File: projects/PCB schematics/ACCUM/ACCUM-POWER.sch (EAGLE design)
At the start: 9 parts, among them J1 2P(90DEG)_1-770966-0, J2 2P(90DEG)_1-770966-0, J3 2P(90DEG)_1-770966-0

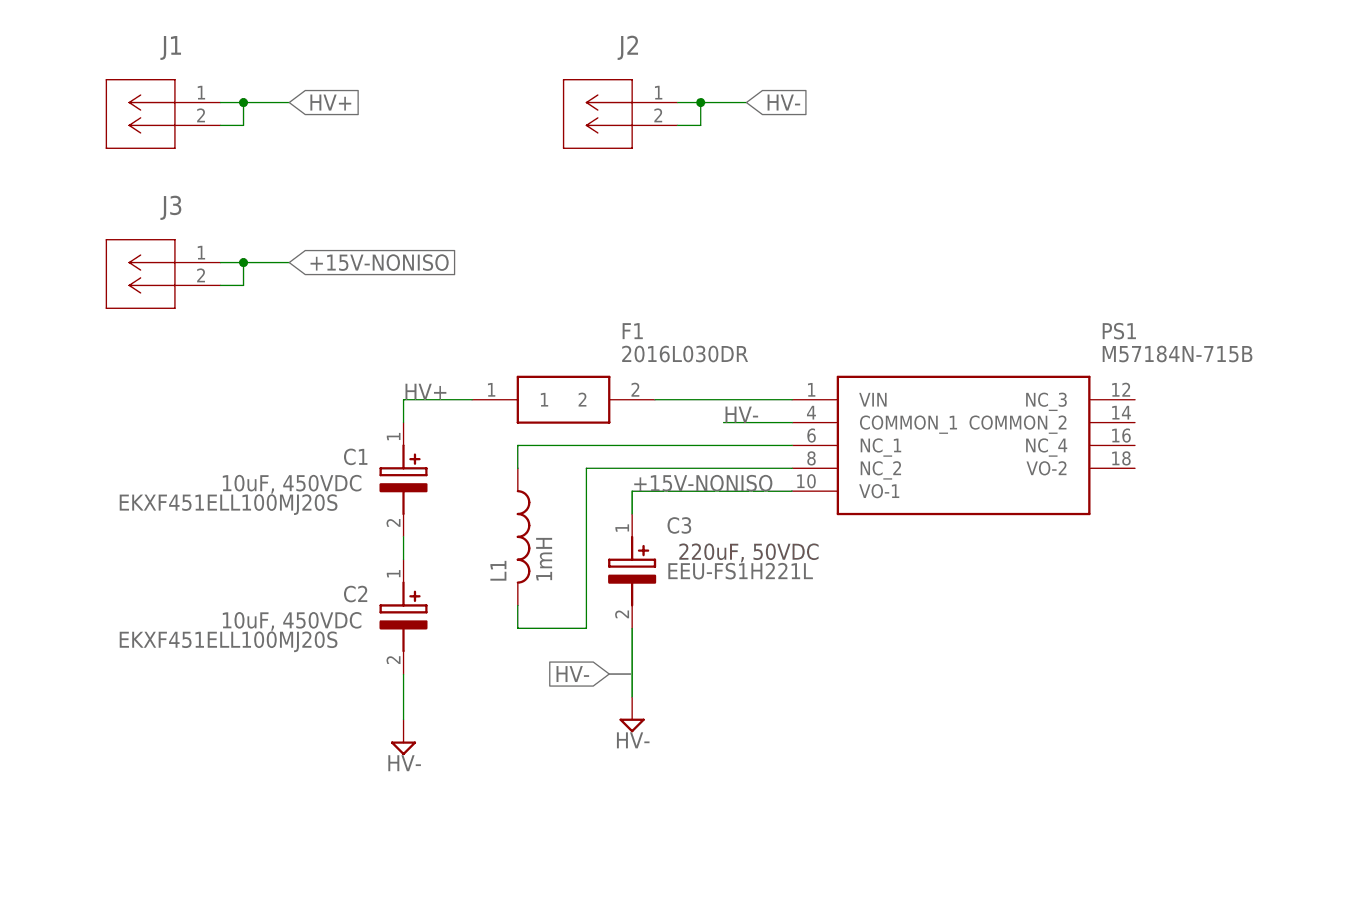
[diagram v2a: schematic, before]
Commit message: TSAL - Added in fuses.
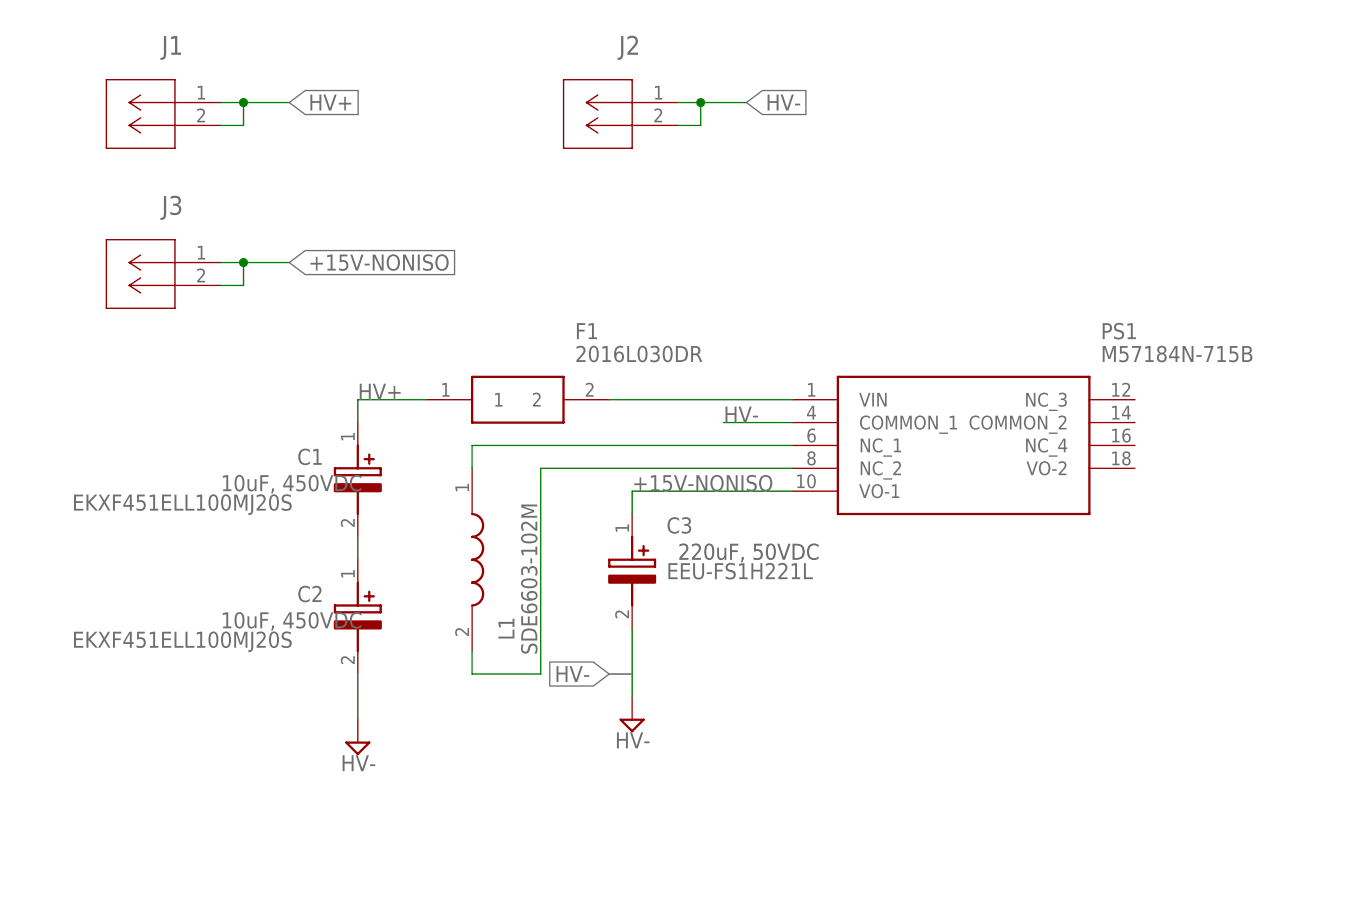
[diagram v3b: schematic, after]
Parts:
- L1: value 1mH -> SDE6603-102M; device rcl:L-USL2012C -> SDE6603-102M:SDE6603-102M
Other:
- moved on the sheet: C1, C2, F1
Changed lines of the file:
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@@
 <parts>
 <part name="PS1" library="M57184N-715B" deviceset="M57184N-715B" device=""/>
-<part name="L1" library="rcl" library_urn="urn:adsk.eagle:library:334" deviceset="L-US" device="L2012C" package3d_urn="urn:adsk.eagle:package:23475/2" value="1mH"/>
 <part name="C3" library="EEU-FS1H221L" deviceset="EEU-FS1H221L" device=""/>
 <part name="SUPPLY16" library="supply2" library_urn="urn:adsk.eagle:library:372" deviceset="GND" device="" value="HV-"/>
@@
 <part name="J3" library="con-MATE-N-LOK" deviceset="2P(90DEG)_1-770966-0" device=""/>
 <part name="F1" library="SamacSys_Parts" deviceset="2016L030DR" device=""/>
+<part name="L1" library="SDE6603-102M" deviceset="SDE6603-102M" device=""/>
 </parts>
 <sheets>
@@
 <attribute name="VALUE" x="118.11" y="63.5" size="1.778" layer="96" align="center-left"/>
 </instance>
-<instance part="L1" gate="G$1" x="53.34" y="43.18" smashed="yes">
-<attribute name="NAME" x="52.07" y="38.1" size="1.778" layer="95" rot="R90"/>
-<attribute name="VALUE" x="57.15" y="38.1" size="1.778" layer="96" rot="R90"/>
-</instance>
 <instance part="C3" gate="G$1" x="66.04" y="45.72" smashed="yes" rot="R270">
 <attribute name="NAME" x="69.85" y="44.45" size="1.778" layer="95" rot="MR180" align="center-left"/>
@@
 <attribute name="VALUE" x="64.135" y="19.685" size="1.778" layer="96"/>
 </instance>
-<instance part="SUPPLY17" gate="GND" x="40.64" y="20.32" smashed="yes">
-<attribute name="VALUE" x="38.735" y="17.145" size="1.778" layer="96"/>
+<instance part="SUPPLY17" gate="GND" x="35.56" y="20.32" smashed="yes">
+<attribute name="VALUE" x="33.655" y="17.145" size="1.778" layer="96"/>
 </instance>
-<instance part="C1" gate="G$1" x="40.64" y="55.88" smashed="yes" rot="R270">
-<attribute name="NAME" x="36.83" y="52.07" size="1.778" layer="95" rot="R180" align="center-left"/>
-<attribute name="VALUE" x="8.89" y="46.99" size="1.778" layer="96" align="center-left"/>
+<instance part="C1" gate="G$1" x="35.56" y="55.88" smashed="yes" rot="R270">
+<attribute name="NAME" x="31.75" y="52.07" size="1.778" layer="95" rot="R180" align="center-left"/>
+<attribute name="VALUE" x="3.81" y="46.99" size="1.778" layer="96" align="center-left"/>
 </instance>
-<instance part="C2" gate="G$1" x="40.64" y="40.64" smashed="yes" rot="R270">
-<attribute name="NAME" x="36.83" y="36.83" size="1.778" layer="95" rot="R180" align="center-left"/>
-<attribute name="VALUE" x="8.89" y="31.75" size="1.778" layer="96" align="center-left"/>
+<instance part="C2" gate="G$1" x="35.56" y="40.64" smashed="yes" rot="R270">
+<attribute name="NAME" x="31.75" y="36.83" size="1.778" layer="95" rot="R180" align="center-left"/>
+<attribute name="VALUE" x="3.81" y="31.75" size="1.778" layer="96" align="center-left"/>
 </instance>
 <instance part="J1" gate="A" x="20.32" y="91.44" smashed="yes" rot="MR0">
@@
 <attribute name="NAME" x="16.1544" y="78.9686" size="2.0828" layer="95" ratio="6" rot="SMR0"/>
 </instance>
-<instance part="F1" gate="G$1" x="48.26" y="58.42" smashed="yes">
-<attribute name="NAME" x="64.77" y="66.04" size="1.778" layer="95" align="center-left"/>
-<attribute name="VALUE" x="64.77" y="63.5" size="1.778" layer="96" align="center-left"/>
+<instance part="F1" gate="G$1" x="43.18" y="58.42" smashed="yes">
+<attribute name="NAME" x="59.69" y="66.04" size="1.778" layer="95" align="center-left"/>
+<attribute name="VALUE" x="59.69" y="63.5" size="1.778" layer="96" align="center-left"/>
+</instance>
+<instance part="L1" gate="G$1" x="48.26" y="50.8" smashed="yes" rot="R270">
+<attribute name="NAME" x="52.07" y="34.29" size="1.778" layer="95" rot="R270" align="center-left"/>
+<attribute name="VALUE" x="54.61" y="46.99" size="1.778" layer="96" rot="R270" align="center-left"/>
 </instance>
 </instances>
@@
 <segment>
 <pinref part="SUPPLY17" gate="GND" pin="GND"/>
-<wire x1="40.64" y1="22.86" x2="40.64" y2="27.94" width="0.1524" layer="91"/>
+<wire x1="35.56" y1="22.86" x2="35.56" y2="27.94" width="0.1524" layer="91"/>
 <pinref part="C2" gate="G$1" pin="-"/>
 </segment>
@@
 <net name="HV+" class="0">
 <segment>
-<label x="40.64" y="58.42" size="1.778" layer="95"/>
-<wire x1="40.64" y1="58.42" x2="40.64" y2="55.88" width="0.1524" layer="91"/>
+<label x="35.56" y="58.42" size="1.778" layer="95"/>
+<wire x1="35.56" y1="58.42" x2="35.56" y2="55.88" width="0.1524" layer="91"/>
 <pinref part="C1" gate="G$1" pin="+"/>
 <pinref part="F1" gate="G$1" pin="1"/>
-<wire x1="48.26" y1="58.42" x2="40.64" y2="58.42" width="0.1524" layer="91"/>
+<wire x1="43.18" y1="58.42" x2="35.56" y2="58.42" width="0.1524" layer="91"/>
 </segment>
 <segment>
@@
 <net name="N$1" class="0">
 <segment>
+<wire x1="48.26" y1="30.48" x2="48.26" y2="27.94" width="0.1524" layer="91"/>
+<wire x1="48.26" y1="27.94" x2="55.88" y2="27.94" width="0.1524" layer="91"/>
+<wire x1="55.88" y1="27.94" x2="55.88" y2="50.8" width="0.1524" layer="91"/>
+<pinref part="PS1" gate="G$1" pin="NC_2"/>
+<wire x1="55.88" y1="50.8" x2="83.82" y2="50.8" width="0.1524" layer="91"/>
 <pinref part="L1" gate="G$1" pin="2"/>
-<wire x1="53.34" y1="35.56" x2="53.34" y2="33.02" width="0.1524" layer="91"/>
-<wire x1="53.34" y1="33.02" x2="60.96" y2="33.02" width="0.1524" layer="91"/>
-<wire x1="60.96" y1="33.02" x2="60.96" y2="50.8" width="0.1524" layer="91"/>
-<pinref part="PS1" gate="G$1" pin="NC_2"/>
-<wire x1="60.96" y1="50.8" x2="83.82" y2="50.8" width="0.1524" layer="91"/>
 </segment>
 </net>
@@
 <segment>
 <pinref part="PS1" gate="G$1" pin="NC_1"/>
-<wire x1="83.82" y1="53.34" x2="53.34" y2="53.34" width="0.1524" layer="91"/>
+<wire x1="83.82" y1="53.34" x2="48.26" y2="53.34" width="0.1524" layer="91"/>
+<wire x1="48.26" y1="53.34" x2="48.26" y2="50.8" width="0.1524" layer="91"/>
 <pinref part="L1" gate="G$1" pin="1"/>
-<wire x1="53.34" y1="53.34" x2="53.34" y2="50.8" width="0.1524" layer="91"/>
 </segment>
 </net>
@@
 <net name="N$3" class="0">
 <segment>
-<wire x1="40.64" y1="43.18" x2="40.64" y2="40.64" width="0.1524" layer="91"/>
+<wire x1="35.56" y1="43.18" x2="35.56" y2="40.64" width="0.1524" layer="91"/>
 <pinref part="C1" gate="G$1" pin="-"/>
 <pinref part="C2" gate="G$1" pin="+"/>
@@
 <pinref part="F1" gate="G$1" pin="2"/>
 <pinref part="PS1" gate="G$1" pin="VIN"/>
-<wire x1="68.58" y1="58.42" x2="83.82" y2="58.42" width="0.1524" layer="91"/>
+<wire x1="63.5" y1="58.42" x2="83.82" y2="58.42" width="0.1524" layer="91"/>
 </segment>
 </net>
@@
 will not be understood (or retained) with this version.
 </note>
-<note version="8.3" severity="warning">
-Since Version 8.3, EAGLE supports the association of 3D packages
-with devices in libraries, schematics, and board files. Those 3D
-packages will not be understood (or retained) with this version.
-</note>
 </compatibility>

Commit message: ACCUM - Added IMD fuses.
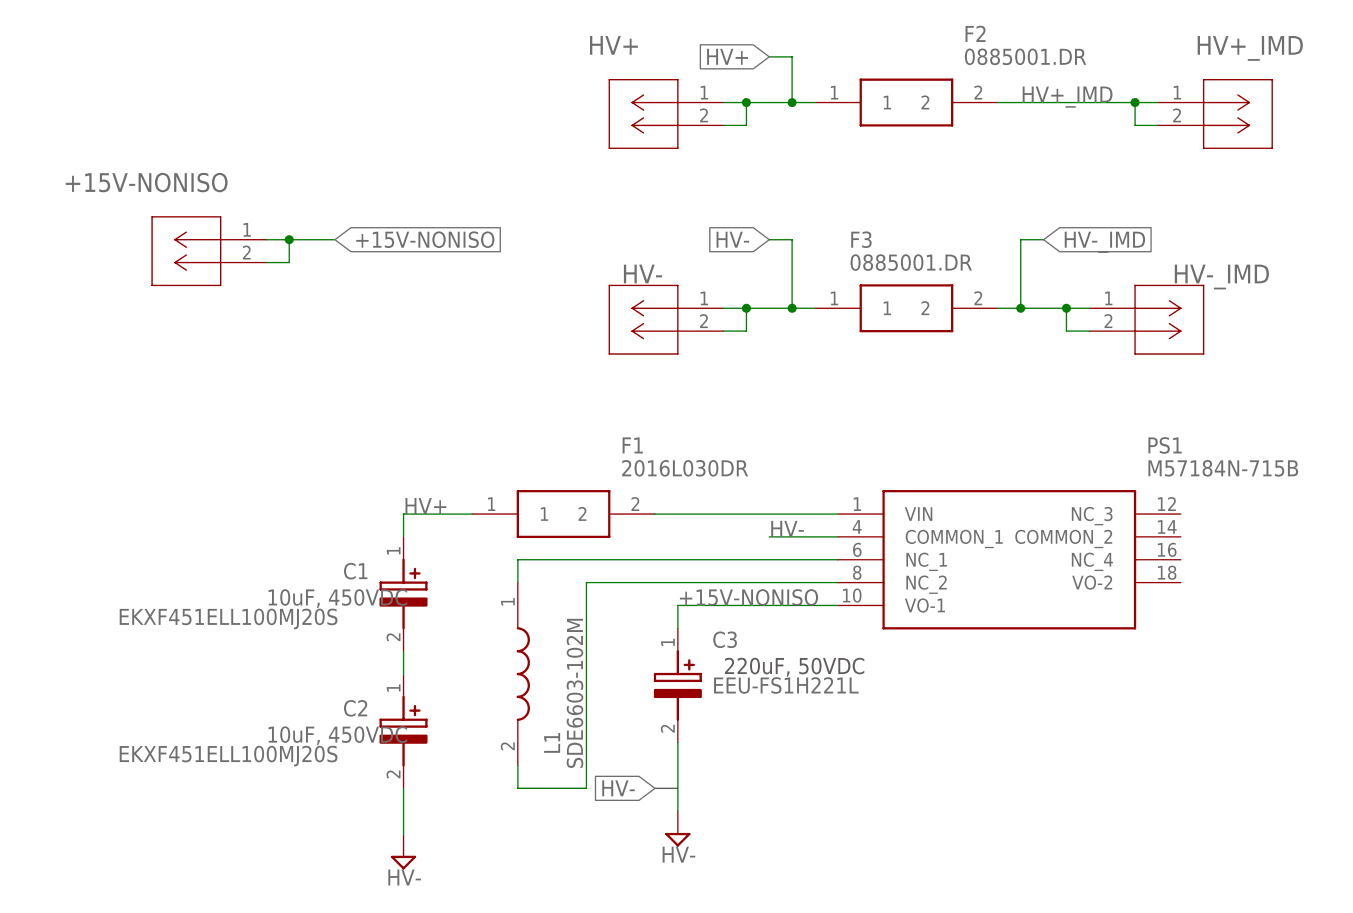
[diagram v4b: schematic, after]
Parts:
- removed J1, J2, J3: 2P(90DEG)_1-770966-0, con-MATE-N-LOK:2P(90DEG)_1-770966-0
- added +15V-NONISO, HV+, HV+_IMD, HV-, HV-_IMD: 2P(90DEG)_1-770966-0, con-MATE-N-LOK:2P(90DEG)_1-770966-0
- added F2, F3: 0885001.DR, 0885001.DR:0885001.DR
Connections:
- new net HV+_IMD: F2.2, HV+_IMD.1, HV+_IMD.2
- new net HV-_IMD: F3.2, HV-_IMD.1, HV-_IMD.2
- net +15V-NONISO: now also +15V-NONISO.1, +15V-NONISO.2; no longer J3.1, J3.2
- net HV+: now also F2.1, HV+.1, HV+.2; no longer J1.1, J1.2
- net HV-: now also F3.1, HV-.1, HV-.2; no longer J2.1, J2.2
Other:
- moved on the sheet: C1, C2, C3, F1, L1, PS1
